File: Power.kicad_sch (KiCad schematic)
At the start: 46 parts, among them J1 DBT50G-9.5-2P, J2 DBT50G-9.5-2P, J3 DBT50G-9.5-2P, J38 2.54-1*4, J4 DBT50G-9.5-2P, U3 TPS63070RNMR

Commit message: Convert to KiCad 10 format
Upgrade the schematics, board and project symbol/footprint libraries with
kicad-cli 10.0.1. The netlist is unchanged (222 nets, 760 pins, 214
components) and ERC/DRC match the KiCad 9 results.

The board used parts from the EasyEDA and PCM_JLCPCB libraries, which were
only in the KiCad 9 global tables on one machine. Copy the parts it uses into
the project and add project table entries under the same nicknames, so no
references change. Clear the PCB's Datasheet "~" placeholders, which
KiCad 10 reports as parity mismatches with the schematic's empty fields.
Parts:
- U4: value ~ -> (none)

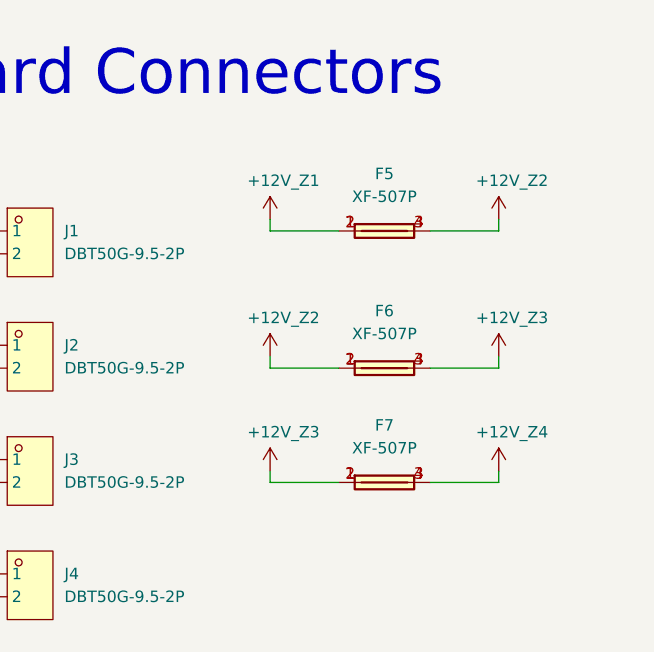
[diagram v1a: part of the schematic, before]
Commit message: Remove zone link fuses F5-F7
They tied supplies in parallel when fitted with more than one input
connected, and capped single-supply operation at one fuse's rating.
They connected only through the B.Cu zone pours, so the zones refill
with no other changes.
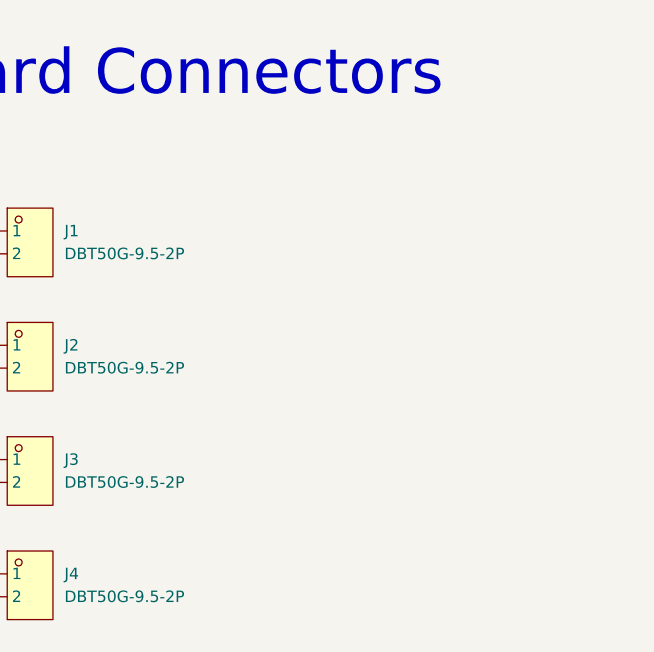
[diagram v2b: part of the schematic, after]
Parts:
- removed F5, F6, F7: XF-507P, JLCImport:XF-507P, symbol JLCImport:XF-507P

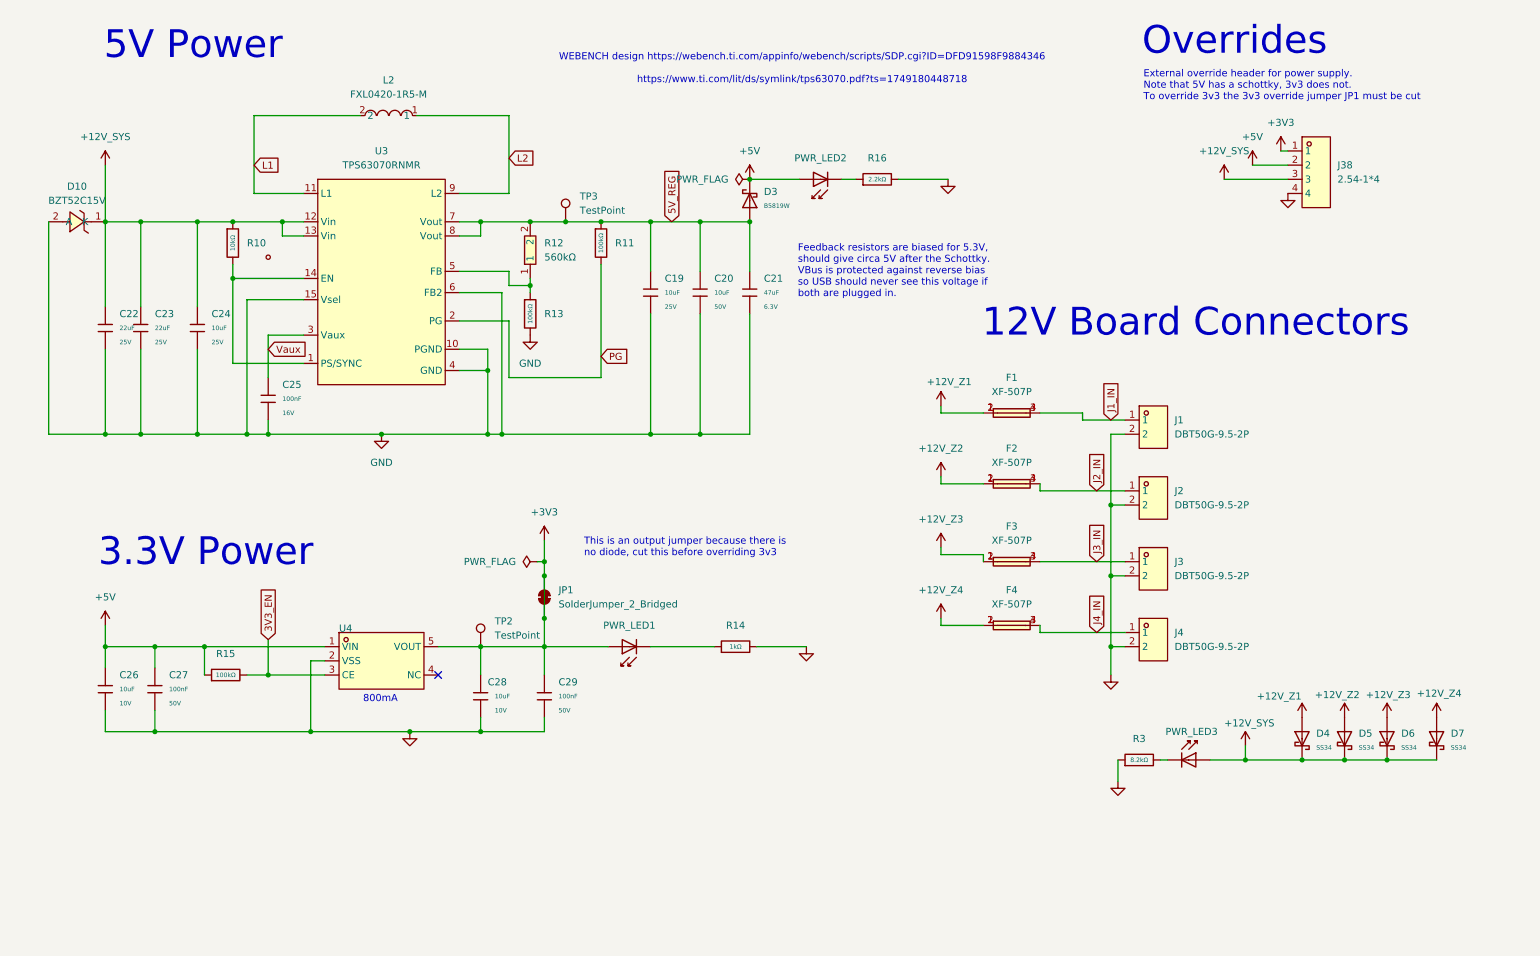
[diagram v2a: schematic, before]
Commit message: Zone silkscreen, 30V port PTCs, string renumbering
- Port PTCs: LUTE 1812L300/30GR (C48985875) imported via jlcimport, pins
  redrawn to match the old symbol; pads unchanged.
- Nets STRINGn/Sn_OUT renumbered by zone (Z1 S0-7 .. Z4 S24-31).
- Silkscreen: S<n>.Z<z> labels, + Zn - on input terminals, zone borders
  following the pours, zone key with voltage write-in, 5-24VDC/VIN labels.
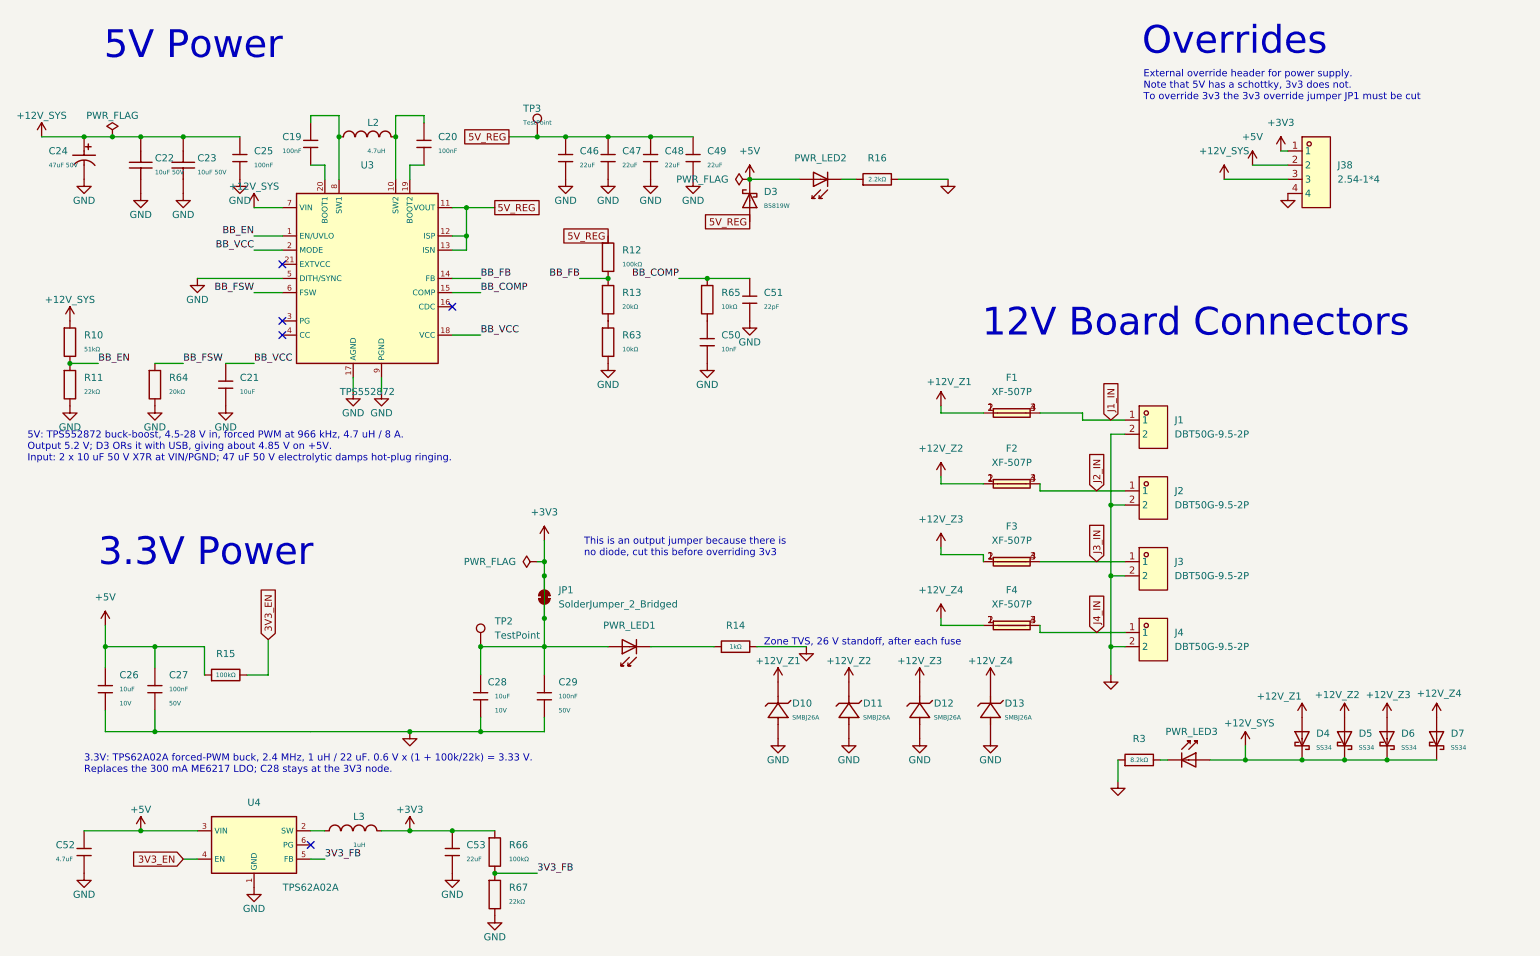
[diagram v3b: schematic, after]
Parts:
- removed C19, C24: 10uF, PixelBlit:C_0603, symbol PixelBlit:0603,10uF,(2)
- removed C20: 10uF, PixelBlit:C_0805, symbol PixelBlit:0805,10uF,(2)
- removed C21: 47uF, PixelBlit:C_0805, symbol PixelBlit:0805,47uF
- removed C22, C23: 22uF, PixelBlit:C_0805, symbol PixelBlit:0805,22uF
- removed C25: 100nF, PixelBlit:C_0402, symbol PixelBlit:0402,100nF
- removed D10: BZT52C15V, EasyEDA:SOD-123_L2.7-W1.6-LS3.7-RD-1, symbol EasyEDA:BZT52C15V
- removed L2: FXL0420-1R5-M, EasyEDA:IND-SMD_L4.4-W4.2, symbol EasyEDA:FXL0420-1R5-M
- removed R10: 10kΩ, PixelBlit:R_0603, symbol PixelBlit:0603,10kΩ
- removed R11, R13: 100kΩ, PixelBlit:R_0603, symbol PixelBlit:0603,100kΩ
- removed R12: 560kΩ, PixelBlit:R0402, symbol PixelBlit:0402WGF5603TCE
- removed U3: TPS63070RNMR, PixelBlit:VQFN-HR-15_L3.0-W2.5-P0.50-BL_TPS63070RNMR, symbol PixelBlit:TPS63070RNMR
- removed U4: (no value), PixelBlit:SOT-23-5_L3.0-W1.7-P0.95-LS2.8-BR, symbol PixelBlit:ME6217C33M5G
- added C19, C20: 100nF, PixelBlit:C_0402, symbol PixelBlit:0402,100nF
- added C21: 10uF, PixelBlit:C_0603, symbol PixelBlit:0603,10uF
- added C22, C23: 10uF 50V, JLCImport:CL31B106KBHNNNE, symbol JLCImport:CL31B106KBHNNNE
- added C24: 47uF 50V, JLCImport:RVT1H470M0607, symbol JLCImport:RVT1H470M0607
- added C25: 100nF, PixelBlit:C_0603, symbol PixelBlit:0603,100nF
- added C46, C47, C48, C49, C53: 22uF, PixelBlit:C_0805, symbol PixelBlit:0805,22uF
- added C50: 10nF, PixelBlit:C_0402, symbol PixelBlit:0402,10nF
- added C51: 22pF, PixelBlit:C_0402, symbol PixelBlit:0402,22pF
- added C52: 4.7uF, PixelBlit:C_0603, symbol PixelBlit:0603,4.7uF
- added D10, D11, D12, D13: SMBJ26A, JLCImport:SMBJ26A_C726831, symbol JLCImport:SMBJ26A_C726831
- added L2: 4.7uH, JLCImport:MWSA0605S-4R7MT, symbol JLCImport:MWSA0605S-4R7MT
- added L3: 1uH, JLCImport:DFE201612E-1R0M_P2, symbol JLCImport:DFE201612E-1R0M_P2
- added R10: 51kΩ, PixelBlit:R_0402, symbol PixelBlit:0402,51kΩ
- added R11, R67: 22kΩ, PixelBlit:R_0402, symbol PixelBlit:0402,22kΩ
- added R12, R66: 100kΩ, PixelBlit:R_0402, symbol PixelBlit:0402,100kΩ
- added R13, R64: 20kΩ, PixelBlit:R_0402, symbol PixelBlit:0402,20kΩ
- added R63, R65: 10kΩ, PixelBlit:R_0402, symbol PixelBlit:0402,10kΩ
- added U3: TPS552872, JLCImport:TPS552872QWRYQRQ1, symbol JLCImport:TPS552872QWRYQRQ1
- added U4: TPS62A02A, JLCImport:TPS62A02ADRLR, symbol JLCImport:TPS62A02ADRLR
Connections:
- net +12V_SYS: now also C22.2, C23.2, C24.1, C25.1, R10.1, U3.7 (VIN)
- net +12V_Z1: now also D10.1 (C)
- net +12V_Z2: now also D11.1 (C)
- net +12V_Z3: now also D12.1 (C)
- net +12V_Z4: now also D13.1 (C)
- net +3V3: now also C53.1, L3.2, R66.1
- net +5V: now also C52.1, U4.3 (VIN)
- net 3V3_EN: now also U4.4 (EN)
- net 5V_REG: now also C46.1, C47.1, C48.1, C49.1, R12.1, U3.11 (VOUT), U3.12 (ISP), U3.13 (ISN)
- net GND: now also C21.2, C22.1, C23.1, C24.2, C25.2, C46.2, C47.2, C48.2, C49.2, C50.2, C51.2, C52.2, C53.2, D10.2 (A), D11.2 (A), D12.2 (A), D13.2 (A), R11.2, R63.2, R64.2, R67.2, U3.17 (AGND), U3.5 (DITH/SYNC), U3.9 (PGND), U4.1 (GND)
- new net: L3.1, U4.2 (SW)
- new net: C20.1, L2.2, U3.10 (SW2)
- new net: C20.2, U3.19 (BOOT2)
- new net: C19.1, L2.1, U3.8 (SW1)
- new net: C19.2, U3.20 (BOOT1)
- new net: R13.2, R63.1
- new net: C50.1, R65.2
- new net 3V3_FB: R66.2, R67.1, U4.5 (FB)
- new net BB_COMP: C51.1, R65.1, U3.15 (COMP)
- new net BB_EN: R10.2, R11.1, U3.1 (EN/UVLO)
- new net BB_FB: R12.2, R13.1, U3.14 (FB)
- new net BB_FSW: R64.1, U3.6 (FSW)
- new net BB_VCC: C21.1, U3.18 (VCC), U3.2 (MODE)
- no-connect marks 1 -> 5
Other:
- note added: "3.3V: TPS62A02A forced-PWM buck, 2.4 MHz, 1 uH / 22 uF. 0.6 V x (1 + 100k/22k) = 3.33 V. Replaces the 300 mA ME6217 LDO; C28 stays at the 3V3 node."
- note added: "5V: TPS552872 buck-boost, 4.5-28 V in, forced PWM at 966 kHz, 4.7 uH / 8 A. Output 5.2 V; D3 ORs it with USB, giving about 4.85 V on +5V. Input: 2 x 10 uF 50 V X7R at VIN/PGND; 47 uF 50 V electrolytic damps hot-plug ringing."
- note added: "Zone TVS, 26 V standoff, after each fuse"
- note removed: "800mA"
- note removed: "Feedback resistors are biased for 5.3V, should give circa 5V after the Schottky. VBus is protected against reverse bias so USB should never see this voltage if both are plugged in."
- note removed: "WEBENCH design https://webench.ti.com/appinfo/webench/scripts/SDP.cgi?ID=DFD91598F9884346 https://www.ti.com/lit/ds/symlink/tps63070.pdf?ts=1749180448718"

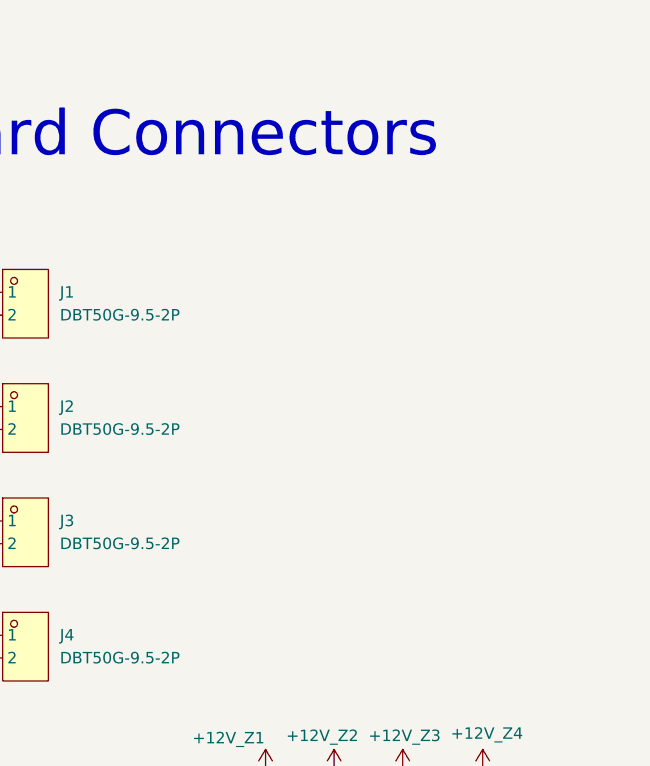
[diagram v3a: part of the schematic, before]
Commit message: Add status RGB LED, user button and blown-fuse LEDs
- D14 common-cathode RGB (C601684) with R72-R74 on GPIO 41/44/45, SW3
  'Play' on GPIO 43; routed from U1 via short F.Cu escapes and In2 lanes
  to the old display area. GPIO 40 and 46 stay spare.
- D15-D18 red LEDs with 10k 0603 across each zone fuse, between holder
  and input terminal.
- Zone borders regenerated; plan doc GPIO map updated.
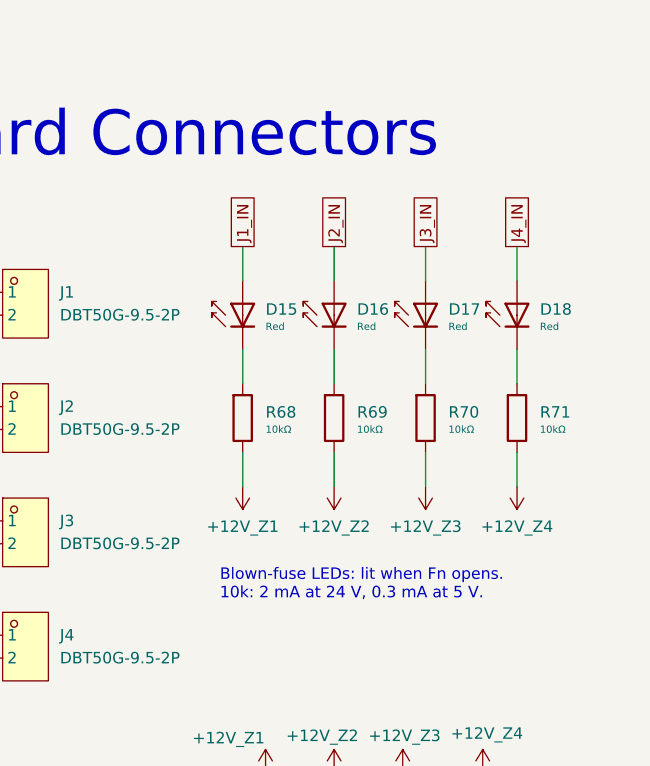
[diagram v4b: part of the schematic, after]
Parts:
- added D15, D16, D17, D18: Red, PixelBlit:D_0603, symbol PixelBlit:LED,0603,Red
- added R68, R69, R70, R71: 10kΩ, PixelBlit:R_0603, symbol PixelBlit:0603,10kΩ
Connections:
- net +12V_Z1: now also R68.2
- net +12V_Z2: now also R69.2
- net +12V_Z3: now also R70.2
- net +12V_Z4: now also R71.2
- net J1_IN: now also D15.2
- net J2_IN: now also D16.2
- net J3_IN: now also D17.2
- net J4_IN: now also D18.2
- new net: D16.1, R69.1
- new net: D17.1, R70.1
- new net: D18.1, R71.1
- new net: D15.1, R68.1
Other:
- note added: "Blown-fuse LEDs: lit when Fn opens. 10k: 2 mA at 24 V, 0.3 mA at 5 V."
